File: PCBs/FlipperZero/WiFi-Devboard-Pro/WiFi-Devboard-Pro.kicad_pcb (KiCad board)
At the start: 2 copper layers, 78.5 x 20.1 mm, 46 parts, among them IC1 ESP32-WROOM-32E-N4, IC2 DMP1045U-7, IC3 AZ1117H-3.3TRE1, IC4 DMP1045U-7, IC5 DMP1045U-7, J1 3220-10-0300-00, J2 X6511WVS-08H-C60D48R2, J3 DZ254S-11-10-48, J4 Conn_01x11, J5 Conn_01x11, J6 503398-1892, U1 MMDT2907A-7-F, U2 MMDT2907A-7-F, U3 MMDT2907A-7-F

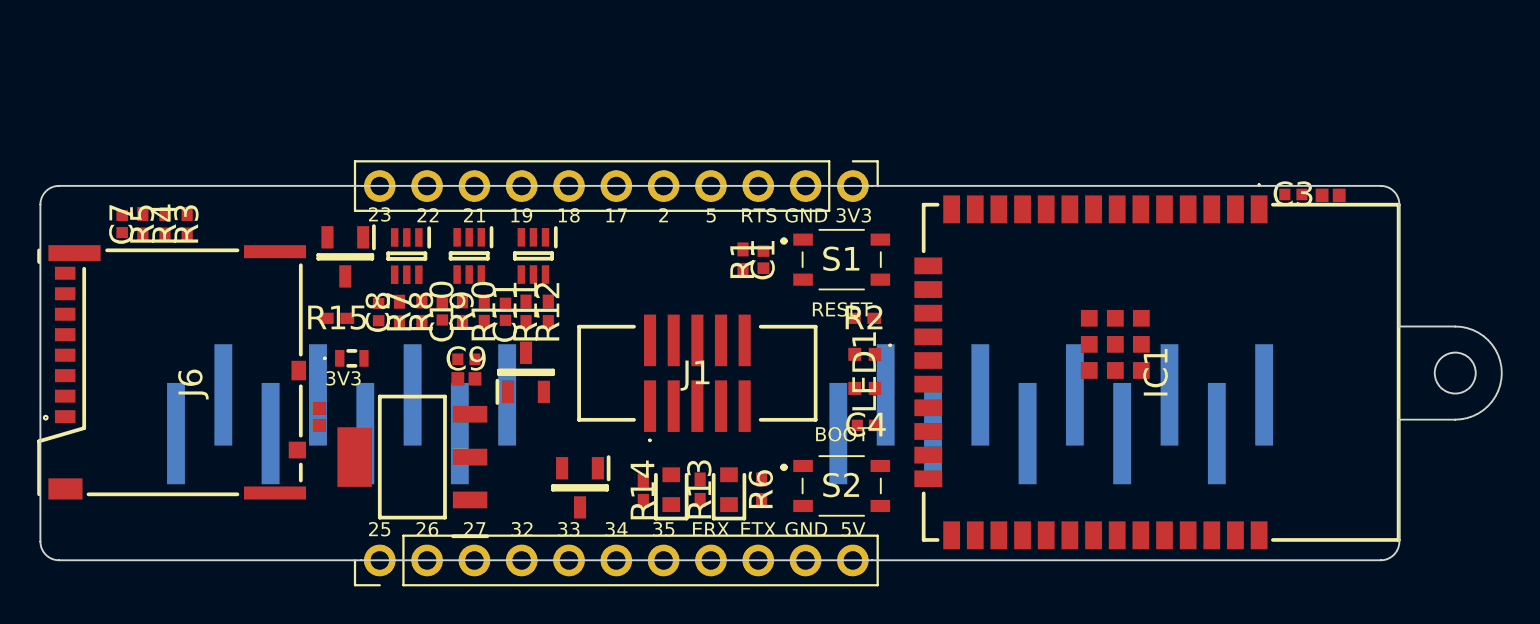
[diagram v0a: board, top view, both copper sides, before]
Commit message: start routing, setting rules
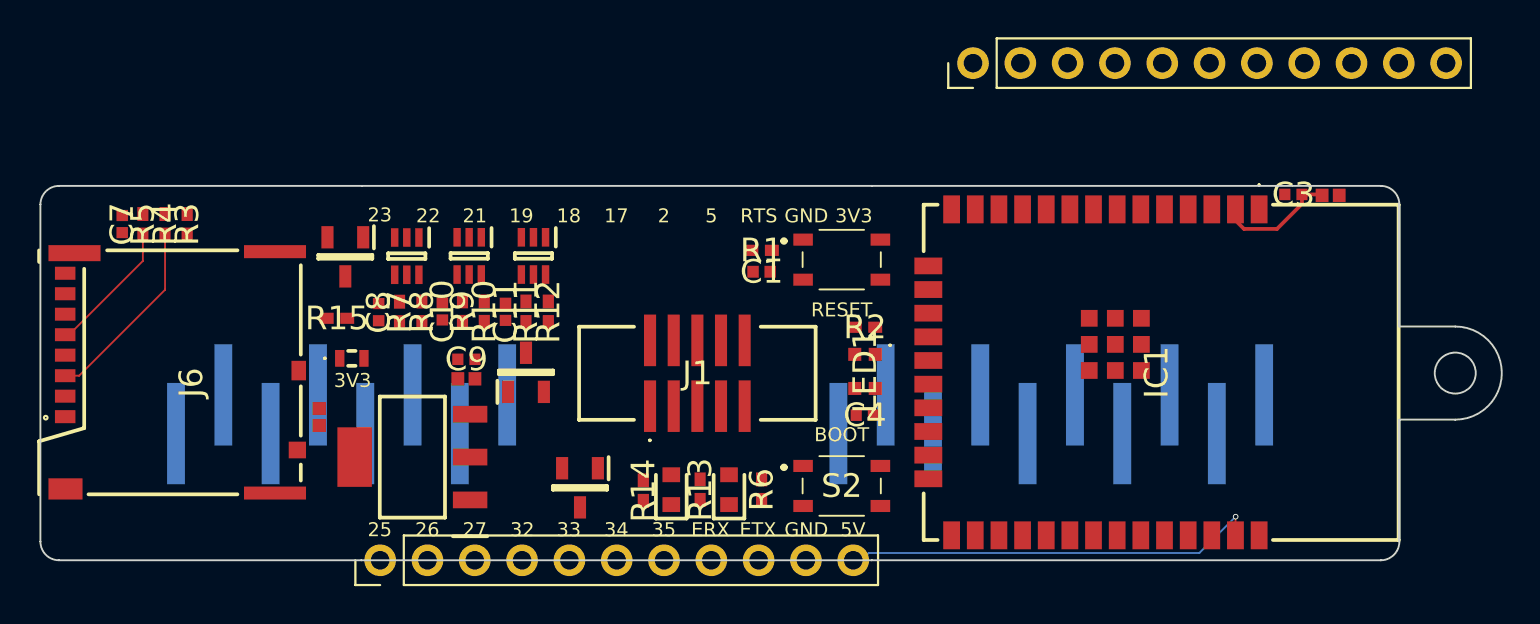
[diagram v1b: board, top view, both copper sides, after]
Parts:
- moved J5 41.6 mm to (161.2, 83.2)
- moved J4 32.4 mm to (129.4, 109.9), turned to 90 degrees
- moved R1 1.12 mm to (149.8, 93.3), turned to 180 degrees
- moved C1 0.66 mm to (149.8, 94.5), turned to 0 degrees
- moved C4 0.55 mm to (155.4, 102.2)
- moved R2 0.48 mm to (155.4, 97.4)
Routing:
- net GPIO23: track 0.00 -> 22.5 mm, vias 0 -> 1
- net Net-(J6-Pad3): track 0.00 -> 10.2 mm
- net Net-(J6-Pad5): track 0.00 -> 7.23 mm
- net +3V3: track 0.00 -> 6.52 mm

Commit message: Start adding traces
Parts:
- moved J5 32.5 mm to (129.3, 89.8)
- moved LED2 13.4 mm to (142.8, 93.8), turned to -90 degrees
- moved R14 13.0 mm to (147.4, 93.8), turned to -90 degrees
- moved R13 12.5 mm to (144.3, 93.8), turned to -90 degrees
- moved LED3 12.3 mm to (145.9, 93.8), turned to -90 degrees
- moved IC4 3.58 mm to (137.2, 103.4), turned to -90 degrees
- moved C6 1.14 mm to (133.1, 99.5), turned to -90 degrees
- moved C7 0.84 mm to (114.9, 91.3), turned to 0 degrees
- moved C9 0.45 mm to (134.3, 99.5), turned to -90 degrees
- moved C11 0.12 mm to (136.2, 96.6)
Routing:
- net +3V3: track 6.52 -> 62.4 mm
- net GPIO05: track 0.00 -> 31.6 mm, vias 0 -> 1
- net GPIO18: track 0.00 -> 31.5 mm, vias 0 -> 2
- net GPIO22: track 0.00 -> 24.8 mm, vias 0 -> 1
- net GPIO17: track 0.00 -> 24.4 mm, vias 0 -> 1
- net GPIO21: track 0.00 -> 23.5 mm, vias 0 -> 1
- net GPIO19: track 0.00 -> 23.4 mm, vias 0 -> 1
- net GPIO02: track 0.00 -> 22.3 mm, vias 0 -> 1
- net +5V: track 0.00 -> 16.8 mm
- net TDO: track 0.00 -> 16.1 mm
- net +LDO_3V3: track 0.00 -> 14.4 mm
- net RX: track 0.00 -> 13.2 mm, vias 0 -> 1
- net Net-(IC1-Pad25): track 0.00 -> 12.5 mm
- net TX: track 0.00 -> 12.5 mm, vias 0 -> 1
- net Net-(J6-Pad2): track 0.00 -> 12.4 mm
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
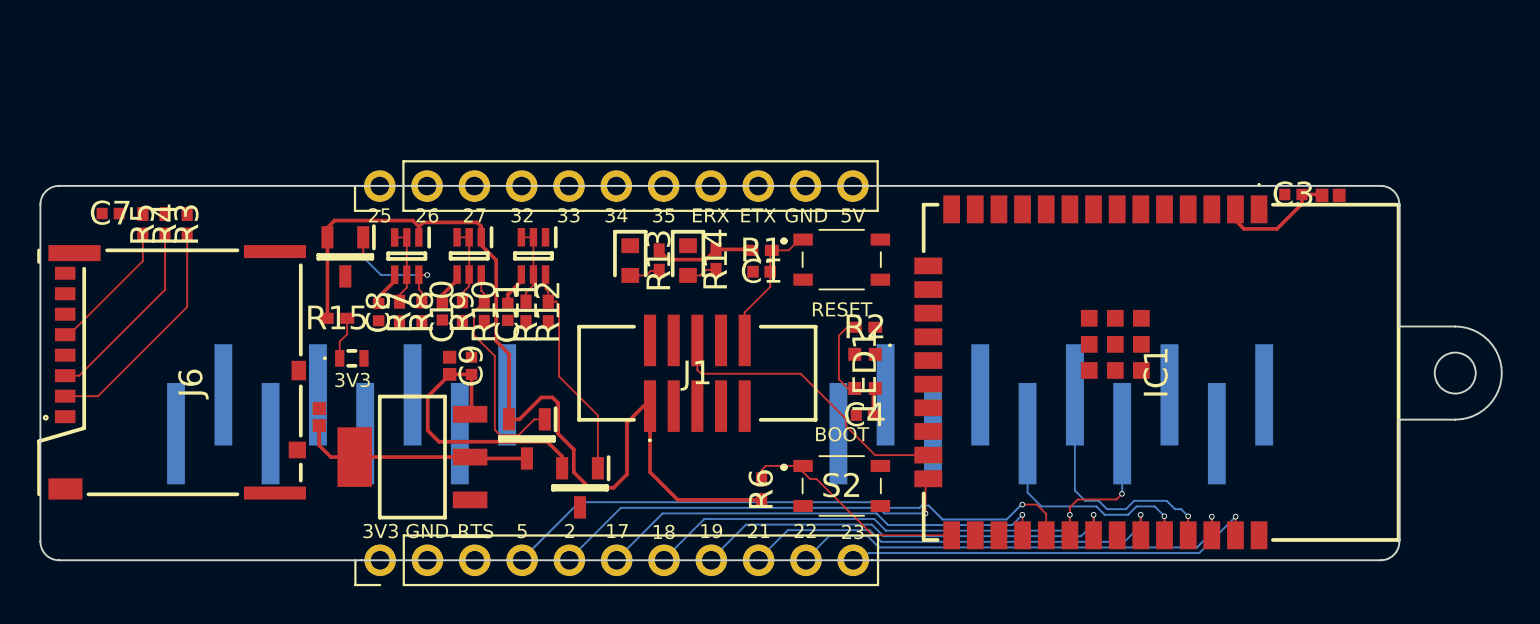
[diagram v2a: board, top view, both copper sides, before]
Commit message: preliminary review done, change RT and TX breakout, add PWR planes 3V3 and GND
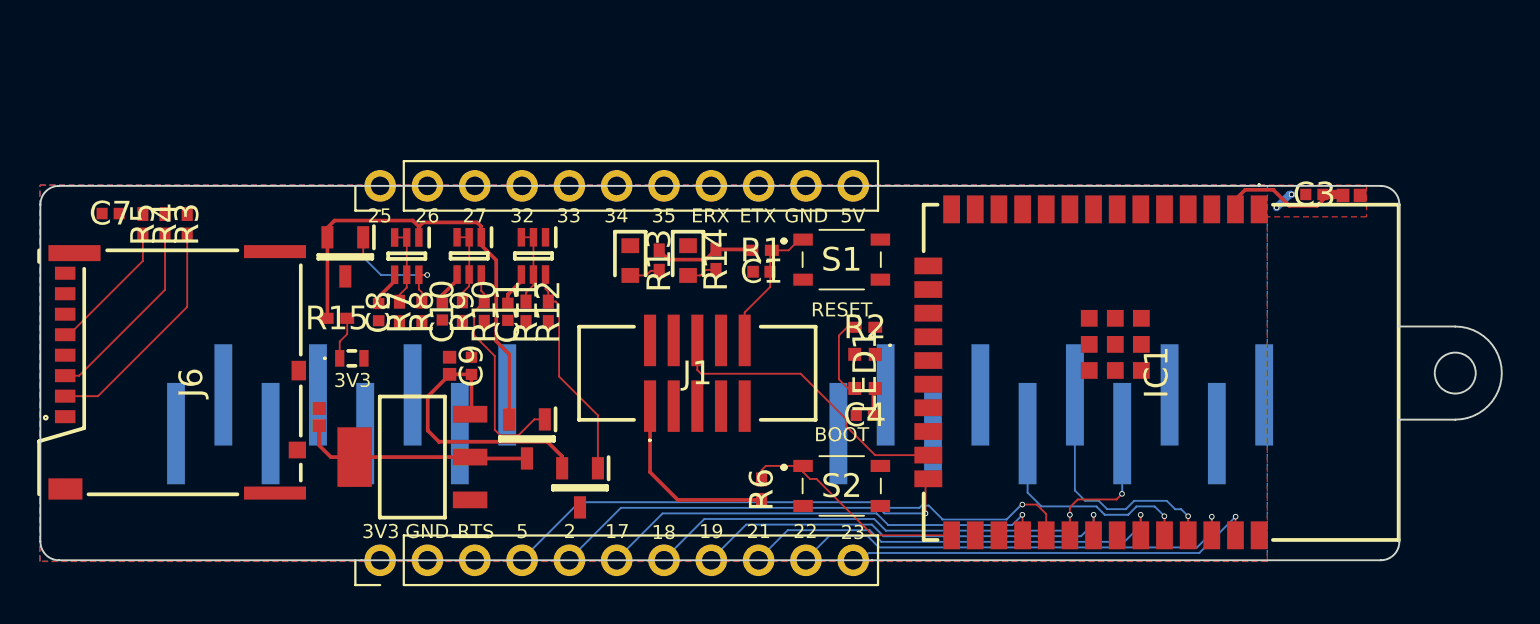
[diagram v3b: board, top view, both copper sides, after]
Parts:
- moved C2 1.12 mm to (181.5, 90.3)
- moved C3 1.12 mm to (179.5, 90.3)
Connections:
- J5 pad 8: TX -> RX
- J5 pad 9: RX -> TX
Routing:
- net +3V3: track 62.4 -> 48.6 mm
- net GND: track 0.00 -> 1.09 mm, vias 0 -> 2
- added copper zone on B.Cu, net +3V3
- added copper zone on F.Cu, net GND

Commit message: Finish all but one connection
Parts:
- moved C7 1.65 mm to (116.5, 91.3), turned to 180 degrees
- moved R5 1.33 mm to (115.3, 91.9)
- moved R1 0.64 mm to (150.2, 93.8)
- moved C1 0.53 mm to (150.3, 94.7)
- moved C10 0.29 mm to (133.0, 96.6)
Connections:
- C4 pad 2: +5V -> +3V3
- LED1 pad 4: +5V -> +3V3
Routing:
- net GPIO04: track 0.00 -> 57.4 mm, vias 0 -> 2
- net GPIO23: track 22.5 -> 79.4 mm, vias 1 -> 3
- net GPIO18: track 31.5 -> 86.7 mm, vias 2 -> 4
- net RX: track 13.2 -> 66.4 mm, vias 1 -> 2
- net +5V: track 16.8 -> 65.4 mm, vias 0 -> 2
- net GPIO19: track 23.4 -> 70.7 mm, vias 1 -> 3
- net RESET: track 7.35 -> 54.6 mm, vias 0 -> 1
- net TX: track 12.5 -> 58.2 mm, vias 1 -> 2
- net +ext_5V: track 2.22 -> 46.7 mm, vias 0 -> 1
- net +ext_3V3: track 1.91 -> 44.0 mm, vias 0 -> 1
- net GPIO25: track 0.00 -> 39.7 mm, vias 0 -> 1
- net GND: track 1.09 -> 38.8 mm, vias 2 -> 17
- net GPIO26: track 0.00 -> 35.5 mm, vias 0 -> 1
- net GPIO32: track 0.00 -> 33.7 mm, vias 0 -> 1
- net GPIO27: track 0.00 -> 31.4 mm, vias 0 -> 1
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
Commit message: Final PCB connection made
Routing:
- net GND: track 38.8 -> 42.1 mm, vias 17 -> 19
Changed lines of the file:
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@@
   (via (at 139.6 98.75) (size 0.3) (drill 0.2) (layers "F.Cu" "B.Cu") (free) (net 1))
   (via (at 128.025 106.8) (size 0.3) (drill 0.2) (layers "F.Cu" "B.Cu") (free) (net 1))
+  (via (at 133.075 98.05) (size 0.3) (drill 0.2) (layers "F.Cu" "B.Cu") (free) (net 1))
+  (via (at 132.95 94.85) (size 0.3) (drill 0.2) (layers "F.Cu" "B.Cu") (free) (net 1))
   (via (at 175.875 101.025) (size 0.3) (drill 0.2) (layers "F.Cu" "B.Cu") (free) (net 1))
   (via (at 135.225 98.175) (size 0.3) (drill 0.2) (layers "F.Cu" "B.Cu") (free) (net 1))
@@
   (segment (start 178.3 90.3) (end 178.2 90.3) (width 0.4) (layer "B.Cu") (net 1))
   (segment (start 149.6 95.975) (end 150.35 95.975) (width 0.2) (layer "B.Cu") (net 1))
+  (segment (start 132.95 97.925) (end 133.075 98.05) (width 0.3) (layer "B.Cu") (net 1))
   (segment (start 156.525 96.35) (end 153.25 96.35) (width 0.2) (layer "B.Cu") (net 1))
   (segment (start 152.725 95.825) (end 150.5 95.825) (width 0.2) (layer "B.Cu") (net 1))
@@
   (segment (start 134.975 98.425) (end 134.975 99.15) (width 0.3) (layer "B.Cu") (net 1))
   (segment (start 123.125 92.2) (end 121.025 92.2) (width 0.3) (layer "B.Cu") (net 1))
+  (segment (start 132.95 94.85) (end 132.95 97.925) (width 0.3) (layer "B.Cu") (net 1))
   (segment (start 178.2 90.3) (end 177.5 91) (width 0.4) (layer "B.Cu") (net 1))
   (segment (start 121.025 92.2) (end 120.975 92.15) (width 0.2) (layer "B.Cu") (net 1))
@@
   (segment (start 179.985 90.3) (end 181.015 90.3) (width 0.5) (layer "F.Cu") (net 3))
   (segment (start 157.225 97.875) (end 157.175 97.925) (width 0.2) (layer "F.Cu") (net 3))
-  (segment (start 131.45 91.775) (end 131.45 92.61) (width 0.2) (layer "F.Cu") (net 3))
   (segment (start 143.25 103.325) (end 143.86 102.715) (width 0.2) (layer "F.Cu") (net 3))
   (segment (start 179.664511 90.909511) (end 178.180489 90.909511) (width 0.2) (layer "F.Cu") (net 3))
@@
   (segment (start 155.30732 102.76) (end 155.53 102.76) (width 0.2) (layer "F.Cu") (net 3))
   (segment (start 136.29 102.16) (end 136.29 102.375) (width 0.2) (layer "F.Cu") (net 3))
+  (segment (start 131.998005 92.351995) (end 131.74 92.61) (width 0.2) (layer "F.Cu") (net 3))
   (segment (start 143.86 102.715) (end 143.86 101.665) (width 0.2) (layer "F.Cu") (net 3))
   (segment (start 126.54 96.91) (end 126.5 96.95) (width 0.2) (layer "F.Cu") (net 3))
+  (segment (start 131.74 92.61) (end 131.45 92.61) (width 0.2) (layer "F.Cu") (net 3))
   (segment (start 181.075 90.36) (end 181.065 90.35) (width 0.2) (layer "F.Cu") (net 3))
   (segment (start 149.125 95.675) (end 149.125 94.35) (width 0.2) (layer "F.Cu") (net 3))
@@
   (via (at 155.259025 102.808295) (size 0.3) (drill 0.2) (layers "F.Cu" "B.Cu") (free) (net 3))
   (via (at 148.825 95.975) (size 0.3) (drill 0.2) (layers "F.Cu" "B.Cu") (free) (net 3))
-  (via (at 131.45 91.775) (size 0.3) (drill 0.2) (layers "F.Cu" "B.Cu") (free) (net 3))
+  (via (at 131.998005 92.351995) (size 0.3) (drill 0.2) (layers "F.Cu" "B.Cu") (free) (net 3))
   (via (at 150.65 97.95) (size 0.3) (drill 0.2) (layers "F.Cu" "B.Cu") (free) (net 3))
   (via (at 144.35 92.6) (size 0.3) (drill 0.2) (layers "F.Cu" "B.Cu") (free) (net 3))
@@
   (segment (start 138.8 96.05) (end 138.975 96.225) (width 0.1) (layer "F.Cu") (net 42))
   (segment (start 141.06 102.16) (end 141.06 105) (width 0.1) (layer "F.Cu") (net 42))
+  (segment (start 123.125 91.175) (end 134.95 91.175) (width 0.2) (layer "F.Cu") (net 43))
   (segment (start 135.615 96.335) (end 135.615 97.84) (width 0.2) (layer "F.Cu") (net 43))
   (segment (start 135.615 97.84) (end 140.1 102.325) (width 0.2) (layer "F.Cu") (net 43))
+  (segment (start 121 93.3) (end 123.125 91.175) (width 0.2) (layer "F.Cu") (net 43))
+  (segment (start 135.425 91.65) (end 135.425 95.34) (width 0.2) (layer "F.Cu") (net 43))
+  (segment (start 136.225 95.675) (end 136.95 94.95) (width 0.2) (layer "F.Cu") (net 43))
+  (segment (start 135.81 96.14) (end 135.615 96.335) (width 0.2) (layer "F.Cu") (net 43))
+  (segment (start 121 94.875) (end 121 93.3) (width 0.2) (layer "F.Cu") (net 43))
+  (segment (start 118.41 100.035) (end 118.41 97.465) (width 0.2) (layer "F.Cu") (net 43))
   (segment (start 118.41 97.465) (end 121 94.875) (width 0.2) (layer "F.Cu") (net 43))
-  (segment (start 121 94.875) (end 121 93.3) (width 0.2) (layer "F.Cu") (net 43))
-  (segment (start 136.225 95.675) (end 136.95 94.95) (width 0.2) (layer "F.Cu") (net 43))
-  (segment (start 122.995 91.305) (end 135.08 91.305) (width 0.2) (layer "F.Cu") (net 43))
-  (segment (start 135.81 96.14) (end 135.615 96.335) (width 0.2) (layer "F.Cu") (net 43))
-  (segment (start 118.41 100.035) (end 118.41 97.465) (width 0.2) (layer "F.Cu") (net 43))
-  (segment (start 135.425 91.65) (end 135.425 95.34) (width 0.2) (layer "F.Cu") (net 43))
   (segment (start 140.1 102.325) (end 140.1 107.1) (width 0.2) (layer "F.Cu") (net 43))
   (segment (start 136.225 96.14) (end 136.225 95.675) (width 0.2) (layer "F.Cu") (net 43))
+  (segment (start 135.425 95.34) (end 136.225 96.14) (width 0.2) (layer "F.Cu") (net 43))
   (segment (start 136.225 96.14) (end 135.81 96.14) (width 0.2) (layer "F.Cu") (net 43))
-  (segment (start 121 93.3) (end 122.995 91.305) (width 0.2) (layer "F.Cu") (net 43))
   (segment (start 136.95 94.95) (end 136.95 94.6) (width 0.2) (layer "F.Cu") (net 43))
   (segment (start 136.95 94.975) (end 136.95 94.6) (width 0.2) (layer "F.Cu") (net 43))
-  (segment (start 135.08 91.305) (end 135.425 91.65) (width 0.2) (layer "F.Cu") (net 43))
-  (segment (start 135.425 95.34) (end 136.225 96.14) (width 0.2) (layer "F.Cu") (net 43))
+  (segment (start 134.95 91.175) (end 135.425 91.65) (width 0.2) (layer "F.Cu") (net 43))
   (via (at 118.41 100.035) (size 0.3) (drill 0.2) (layers "F.Cu" "B.Cu") (net 43))
   (segment (start 118.41 103.14) (end 118.41 100.035) (width 0.2) (layer "B.Cu") (net 43))
